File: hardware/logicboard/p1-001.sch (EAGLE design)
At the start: 25 parts, among them IC1 74LS07N

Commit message: Layout.
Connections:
- net SCL: now also I2C.3; no longer I2C.4
- net SDA: now also I2C.4; no longer I2C.3
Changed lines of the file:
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@@
 <setting verticaltext="up"/>
 </settings>
-<grid distance="0.1" unitdist="inch" unit="inch" style="dots" multiple="1" display="yes" altdistance="0.01" altunitdist="inch" altunit="inch"/>
+<grid distance="0.1" unitdist="inch" unit="inch" style="lines" multiple="1" display="no" altdistance="0.01" altunitdist="inch" altunit="inch"/>
 <layers>
 <layer number="1" name="Top" color="4" fill="1" visible="no" active="no"/>
@@
 <pinref part="I2CSW" gate="A" pin="1"/>
 <wire x1="91.44" y1="50.8" x2="104.14" y2="50.8" width="0.1524" layer="91"/>
-<wire x1="91.44" y1="88.9" x2="91.44" y2="50.8" width="0.1524" layer="91"/>
+<wire x1="91.44" y1="86.36" x2="91.44" y2="50.8" width="0.1524" layer="91"/>
 <junction x="91.44" y="50.8"/>
-<pinref part="I2C" gate="G$1" pin="3"/>
-<wire x1="119.38" y1="88.9" x2="91.44" y2="88.9" width="0.1524" layer="91"/>
+<pinref part="I2C" gate="G$1" pin="4"/>
+<wire x1="91.44" y1="86.36" x2="119.38" y2="86.36" width="0.1524" layer="91"/>
+<label x="109.22" y="86.36" size="1.778" layer="95"/>
 </segment>
 </net>
@@
 <pinref part="I2CSW" gate="A" pin="3"/>
 <wire x1="93.98" y1="53.34" x2="104.14" y2="53.34" width="0.1524" layer="91"/>
-<wire x1="93.98" y1="86.36" x2="93.98" y2="53.34" width="0.1524" layer="91"/>
+<wire x1="93.98" y1="88.9" x2="93.98" y2="53.34" width="0.1524" layer="91"/>
 <junction x="93.98" y="53.34"/>
-<pinref part="I2C" gate="G$1" pin="4"/>
-<wire x1="119.38" y1="86.36" x2="93.98" y2="86.36" width="0.1524" layer="91"/>
+<pinref part="I2C" gate="G$1" pin="3"/>
+<wire x1="93.98" y1="88.9" x2="119.38" y2="88.9" width="0.1524" layer="91"/>
+<label x="109.22" y="88.9" size="1.778" layer="95"/>
 </segment>
 </net>
@@
 <wire x1="99.06" y1="63.5" x2="99.06" y2="91.44" width="0.1524" layer="91"/>
 <junction x="99.06" y="63.5"/>
-</segment>
-</net>
+<label x="109.22" y="91.44" size="1.778" layer="95"/>
+</segment>
+</net>

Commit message: New silk.
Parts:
- added VOUT: (no value), pinhead:PINHD-1X3
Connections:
- new net 3V: U$1.3V, VOUT.1, VOUT.2
- net GND: now also VOUT.3
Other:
- moved on the sheet: CH, D1, IC1A, IN, LD, OK1, R2, R3, R4, THRU, XLD

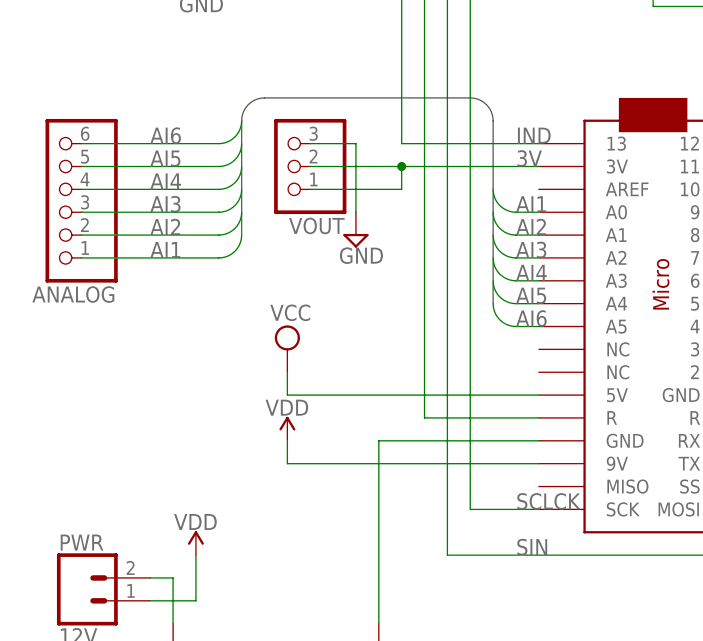
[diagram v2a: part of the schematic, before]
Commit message: Vcc and Vref terminal.
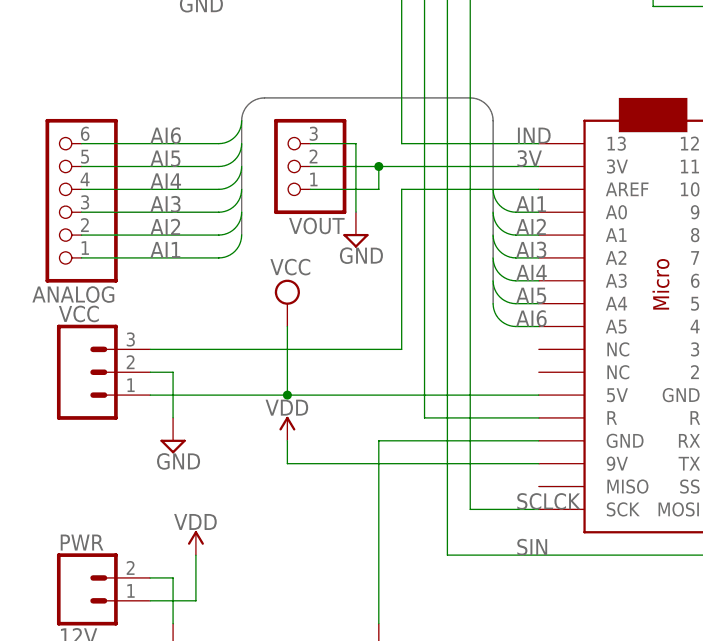
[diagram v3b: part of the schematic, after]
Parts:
- added VCC: (no value), SparkFun-Connectors:CONN_03JST-PTH-VERT
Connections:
- new net VREF: U$1.AREF, VCC.3
- net GND: now also VCC.2
- net VCC: now also VCC.1
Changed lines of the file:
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@@
 <part name="VOUT" library="pinhead" library_urn="urn:adsk.eagle:library:325" deviceset="PINHD-1X3" device="" package3d_urn="urn:adsk.eagle:package:22458/2"/>
 <part name="$1_39_$_2018-07-15_07-03-01" library="supply2" library_urn="urn:adsk.eagle:library:372" deviceset="GND" device=""/>
+<part name="VCC" library="SparkFun-Connectors" library_urn="urn:adsk.eagle:library:513" deviceset="CONN_03" device="JST-PTH-VERT" package3d_urn="urn:adsk.eagle:package:38080/1"/>
+<part name="$1_52_$_2018-07-15_07-03-01" library="supply2" library_urn="urn:adsk.eagle:library:372" deviceset="GND" device=""/>
 </parts>
 <sheets>
@@
 <instance part="IC1" gate="C" x="226.06" y="66.04"/>
 <instance part="D1" gate="G$1" x="180.34" y="43.18" rot="MR90"/>
-<instance part="SUPPLY14" gate="G$1" x="22.86" y="53.34"/>
+<instance part="SUPPLY14" gate="G$1" x="22.86" y="58.42"/>
 <instance part="$1_39_$_2018-07-15_07-03-06" gate="GND" x="33.02" y="20.32"/>
 <instance part="IN" gate="G$1" x="208.28" y="40.64" rot="R180"/>
@@
 <instance part="VOUT" gate="A" x="22.86" y="73.66" rot="R180"/>
 <instance part="$1_39_$_2018-07-15_07-03-01" gate="GND" x="30.48" y="66.04"/>
+<instance part="VCC" gate="J$1" x="0" y="50.8"/>
+<instance part="$1_52_$_2018-07-15_07-03-01" gate="GND" x="10.16" y="43.18"/>
 </instances>
 <busses>
@@
 <wire x1="30.48" y1="76.2" x2="30.48" y2="68.58" width="0.1524" layer="91"/>
 </segment>
+<segment>
+<pinref part="VCC" gate="J$1" pin="2"/>
+<wire x1="7.62" y1="50.8" x2="10.16" y2="50.8" width="0.1524" layer="91"/>
+<pinref part="$1_52_$_2018-07-15_07-03-01" gate="GND" pin="GND"/>
+<wire x1="10.16" y1="50.8" x2="10.16" y2="45.72" width="0.1524" layer="91"/>
+</segment>
 </net>
 <net name="VCC" class="0">
@@
 <segment>
 <pinref part="SUPPLY14" gate="G$1" pin="VCC"/>
-<wire x1="22.86" y1="50.8" x2="22.86" y2="48.26" width="0.1524" layer="91"/>
+<wire x1="22.86" y1="55.88" x2="22.86" y2="48.26" width="0.1524" layer="91"/>
 <pinref part="U$1" gate="G$1" pin="5V"/>
 <wire x1="22.86" y1="48.26" x2="50.8" y2="48.26" width="0.1524" layer="91"/>
+<pinref part="VCC" gate="J$1" pin="1"/>
+<wire x1="22.86" y1="48.26" x2="7.62" y2="48.26" width="0.1524" layer="91"/>
+<junction x="22.86" y="48.26"/>
 </segment>
 <segment>
@@
 <segment>
 <pinref part="U$1" gate="G$1" pin="3V"/>
-<wire x1="50.8" y1="73.66" x2="35.56" y2="73.66" width="0.1524" layer="91"/>
-<wire x1="35.56" y1="73.66" x2="25.4" y2="73.66" width="0.1524" layer="91"/>
-<wire x1="35.56" y1="73.66" x2="35.56" y2="71.12" width="0.1524" layer="91"/>
-<junction x="35.56" y="73.66"/>
-<wire x1="35.56" y1="71.12" x2="25.4" y2="71.12" width="0.1524" layer="91"/>
+<wire x1="50.8" y1="73.66" x2="33.02" y2="73.66" width="0.1524" layer="91"/>
+<wire x1="33.02" y1="73.66" x2="25.4" y2="73.66" width="0.1524" layer="91"/>
+<wire x1="33.02" y1="73.66" x2="33.02" y2="71.12" width="0.1524" layer="91"/>
+<junction x="33.02" y="73.66"/>
+<wire x1="33.02" y1="71.12" x2="25.4" y2="71.12" width="0.1524" layer="91"/>
 <pinref part="VOUT" gate="A" pin="1"/>
 <pinref part="VOUT" gate="A" pin="2"/>
@@
 </segment>
 </net>
+<net name="VREF" class="0">
+<segment>
+<pinref part="U$1" gate="G$1" pin="AREF"/>
+<wire x1="50.8" y1="71.12" x2="35.56" y2="71.12" width="0.1524" layer="91"/>
+<wire x1="35.56" y1="71.12" x2="35.56" y2="53.34" width="0.1524" layer="91"/>
+<pinref part="VCC" gate="J$1" pin="3"/>
+<wire x1="35.56" y1="53.34" x2="7.62" y2="53.34" width="0.1524" layer="91"/>
+</segment>
+</net>

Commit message: Silk.
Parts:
- renumbered PWR to PWR12V, VCC to VCC/VREF
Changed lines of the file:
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@@
 <part name="PWMDRV" library="SparkFun-Retired" deviceset="TLC5940" device="-NT"/>
 <part name="$1_43_$_2018-07-15_07-03-06" library="supply2" library_urn="urn:adsk.eagle:library:372" deviceset="GND" device=""/>
-<part name="PWR" library="SparkFun-Connectors" deviceset="CONN_02" device="JST-PTH-2" value="12V"/>
+<part name="PWR12V" library="SparkFun-Connectors" deviceset="CONN_02" device="JST-PTH-2" value="12V"/>
 <part name="$1_51_$_2018-07-15_07-03-06" library="SparkFun-PowerSymbols" deviceset="VDD" device=""/>
 <part name="SUPPLY12" library="SparkFun-PowerSymbols" deviceset="VDD" device=""/>
@@
 <part name="VOUT" library="pinhead" library_urn="urn:adsk.eagle:library:325" deviceset="PINHD-1X3" device="" package3d_urn="urn:adsk.eagle:package:22458/2"/>
 <part name="$1_39_$_2018-07-15_07-03-01" library="supply2" library_urn="urn:adsk.eagle:library:372" deviceset="GND" device=""/>
-<part name="VCC" library="SparkFun-Connectors" library_urn="urn:adsk.eagle:library:513" deviceset="CONN_03" device="JST-PTH-VERT" package3d_urn="urn:adsk.eagle:package:38080/1"/>
+<part name="VCC/VREF" library="SparkFun-Connectors" library_urn="urn:adsk.eagle:library:513" deviceset="CONN_03" device="JST-PTH-VERT" package3d_urn="urn:adsk.eagle:package:38080/1"/>
 <part name="$1_52_$_2018-07-15_07-03-01" library="supply2" library_urn="urn:adsk.eagle:library:372" deviceset="GND" device=""/>
 </parts>
@@
 <instance part="PWMDRV" gate="G$1" x="76.2" y="119.38" rot="R90"/>
 <instance part="$1_43_$_2018-07-15_07-03-06" gate="GND" x="96.52" y="101.6"/>
-<instance part="PWR" gate="G$1" x="0" y="25.4"/>
+<instance part="PWR12V" gate="G$1" x="0" y="25.4"/>
 <instance part="$1_51_$_2018-07-15_07-03-06" gate="VDD" x="12.7" y="30.48"/>
 <instance part="SUPPLY12" gate="VDD" x="22.86" y="43.18"/>
@@
 <instance part="VOUT" gate="A" x="22.86" y="73.66" rot="R180"/>
 <instance part="$1_39_$_2018-07-15_07-03-01" gate="GND" x="30.48" y="66.04"/>
-<instance part="VCC" gate="J$1" x="0" y="50.8"/>
+<instance part="VCC/VREF" gate="J$1" x="0" y="50.8"/>
 <instance part="$1_52_$_2018-07-15_07-03-01" gate="GND" x="10.16" y="43.18"/>
 </instances>
@@
 </segment>
 <segment>
-<pinref part="PWR" gate="G$1" pin="2"/>
+<pinref part="PWR12V" gate="G$1" pin="2"/>
 <wire x1="7.62" y1="27.94" x2="10.16" y2="27.94" width="0.1524" layer="91"/>
 <pinref part="$1_52_$_2018-07-15_07-03-06" gate="GND" pin="GND"/>
@@
 </segment>
 <segment>
-<pinref part="VCC" gate="J$1" pin="2"/>
+<pinref part="VCC/VREF" gate="J$1" pin="2"/>
 <wire x1="7.62" y1="50.8" x2="10.16" y2="50.8" width="0.1524" layer="91"/>
 <pinref part="$1_52_$_2018-07-15_07-03-01" gate="GND" pin="GND"/>
@@
 <pinref part="U$1" gate="G$1" pin="5V"/>
 <wire x1="22.86" y1="48.26" x2="50.8" y2="48.26" width="0.1524" layer="91"/>
-<pinref part="VCC" gate="J$1" pin="1"/>
+<pinref part="VCC/VREF" gate="J$1" pin="1"/>
 <wire x1="22.86" y1="48.26" x2="7.62" y2="48.26" width="0.1524" layer="91"/>
 <junction x="22.86" y="48.26"/>
@@
 <pinref part="$1_51_$_2018-07-15_07-03-06" gate="VDD" pin="VDD"/>
 <wire x1="12.7" y1="30.48" x2="12.7" y2="25.4" width="0.1524" layer="91"/>
-<pinref part="PWR" gate="G$1" pin="1"/>
+<pinref part="PWR12V" gate="G$1" pin="1"/>
 <wire x1="12.7" y1="25.4" x2="7.62" y2="25.4" width="0.1524" layer="91"/>
 </segment>
@@
 <wire x1="50.8" y1="71.12" x2="35.56" y2="71.12" width="0.1524" layer="91"/>
 <wire x1="35.56" y1="71.12" x2="35.56" y2="53.34" width="0.1524" layer="91"/>
-<pinref part="VCC" gate="J$1" pin="3"/>
+<pinref part="VCC/VREF" gate="J$1" pin="3"/>
 <wire x1="35.56" y1="53.34" x2="7.62" y2="53.34" width="0.1524" layer="91"/>
 </segment>
